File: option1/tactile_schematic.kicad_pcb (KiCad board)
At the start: 2 copper layers, 89.3 x 58.4 mm, 37 parts, among them IC1 CY8C4145PVI-PS431, J1 Conn_01x02, J2 Conn_01x04, J3 Conn_01x04, J4 Conn_01x02

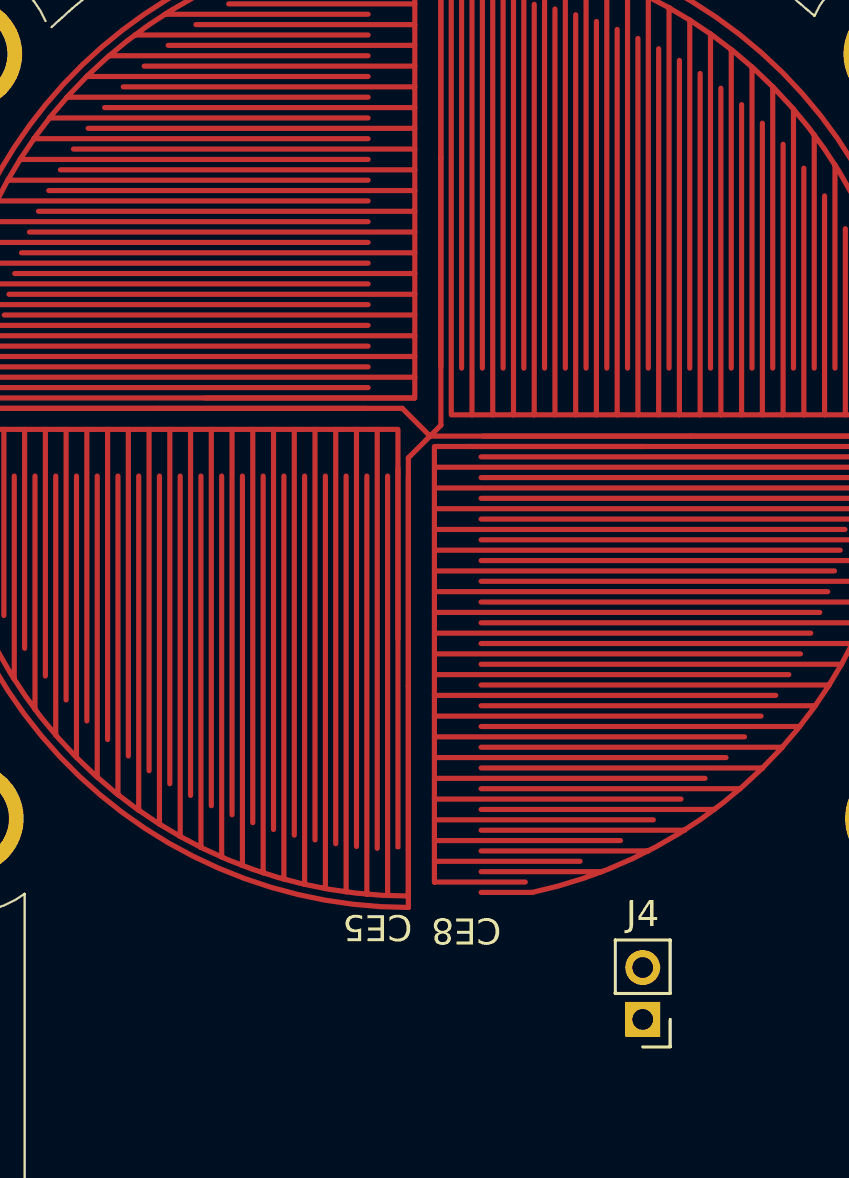
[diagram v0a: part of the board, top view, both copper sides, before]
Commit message: need to fix edge cuts not lining up
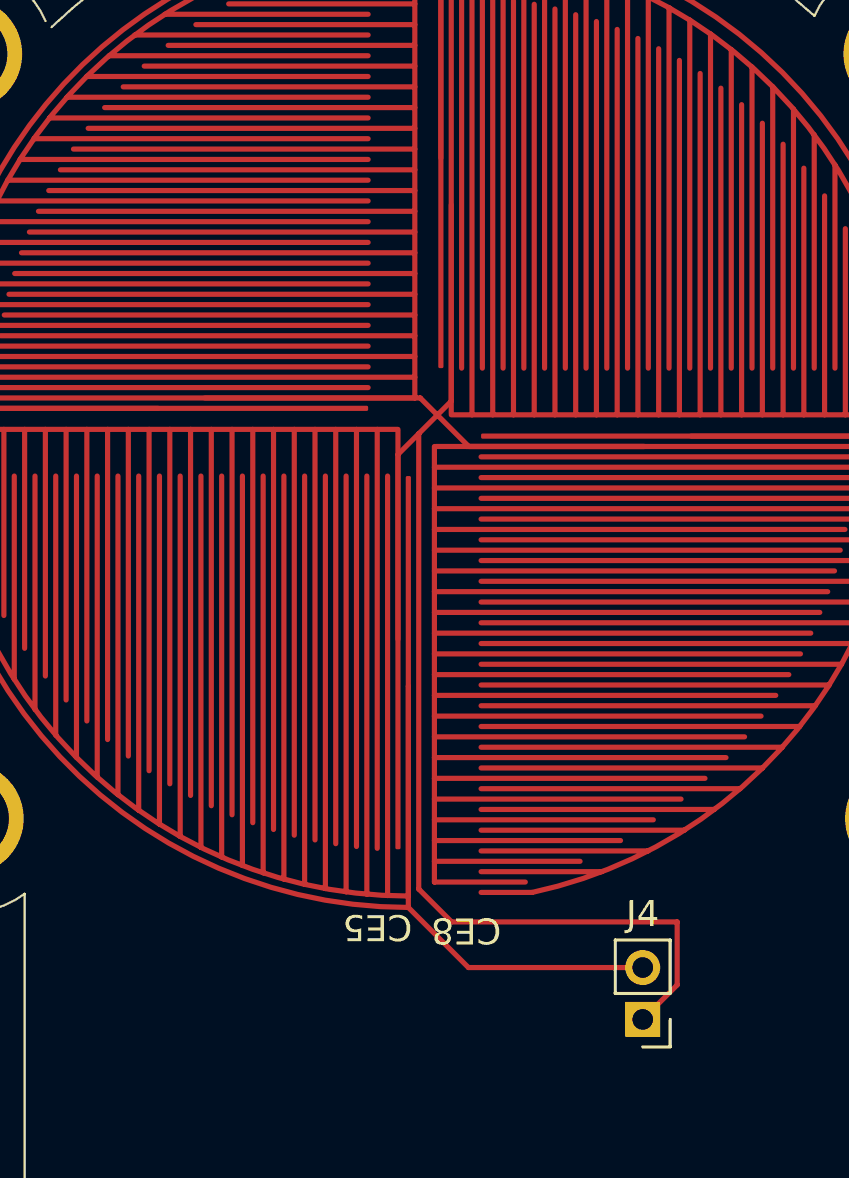
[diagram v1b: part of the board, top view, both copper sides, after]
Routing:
- net P5.2: track 30.3 -> 83.3 mm
- net P5.3: track 96.5 -> 64.7 mm
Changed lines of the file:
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@@
-	)
-	(segment
-		(start 242.08072 51.9999)
-		(end 242.91862 51.162)
-		(width 0.2)
-		(layer "F.Cu")
-		(net 5)
-	)
-	(segment
-		(start 243.33572 40.441)
-		(end 243.33572 50.7449)
-		(width 0.2)
-		(layer "F.Cu")
-		(net 5)
 	)
 	(segment
@@
 	)
 	(segment
-		(start 242.91862 51.162)
-		(end 252.98572 51.162)
-		(width 0.2)
-		(layer "F.Cu")
-		(net 5)
-	)
-	(segment
 		(start 223.908189 49.797789)
 		(end 223.8944 49.784)
@@
 	)
 	(segment
-		(start 243.33572 50.7449)
-		(end 242.91862 51.162)
-		(width 0.2)
-		(layer "F.Cu")
-		(net 5)
-	)
-	(segment
 		(start 243.33572 32.0548)
 		(end 238.5248 32.0548)
@@
 	(segment
 		(start 242.08072 60.802)
-		(end 242.08072 51.9999)
-		(width 0.2)
-		(layer "F.Cu")
-		(net 5)
-	)
-	(segment
-		(start 242.08072 60.802)
 		(end 242.0808 60.80208)
+		(width 0.2)
+		(layer "F.Cu")
+		(net 5)
+	)
+	(segment
+		(start 244.39872 71.66)
+		(end 242.08072 69.342)
 		(width 0.2)
 		(layer "F.Cu")
@@
 	)
 	(segment
+		(start 251.121 71.66)
+		(end 244.39872 71.66)
+		(width 0.2)
+		(layer "F.Cu")
+		(net 5)
+	)
+	(segment
 		(start 204.231 73.55)
 		(end 206.121 71.66)
@@
 	)
 	(segment
-		(start 241.84762 50.091)
-		(end 242.91862 51.162)
-		(width 0.2)
-		(layer "F.Cu")
-		(net 5)
-	)
-	(segment
-		(start 232.43072 50.091)
-		(end 241.84762 50.091)
-		(width 0.2)
-		(layer "F.Cu")
-		(net 5)
+		(start 243.73572 42.243)
+		(end 243.73572 49.81428)
+		(width 0.2)
+		(layer "F.Cu")
+		(net 6)
 	)
 	(segment
@@
 	)
 	(segment
-		(start 242.318 49.691)
-		(end 234.23272 49.691)
-		(width 0.2)
-		(layer "F.Cu")
-		(net 6)
-	)
-	(segment
-		(start 241.68072 52.3999)
-		(end 241.68072 59)
+		(start 243.2 50.35)
+		(end 244.412 51.562)
+		(width 0.2)
+		(layer "F.Cu")
+		(net 6)
+	)
+	(segment
+		(start 244.412 51.562)
+		(end 251.18372 51.562)
+		(width 0.2)
+		(layer "F.Cu")
+		(net 6)
+	)
+	(segment
+		(start 241.68072 59)
+		(end 241.68072 51.86928)
+		(width 0.2)
+		(layer "F.Cu")
+		(net 6)
+	)
+	(segment
+		(start 242.48172 51.08172)
+		(end 242.48172 68.63172)
+		(width 0.2)
+		(layer "F.Cu")
+		(net 6)
+	)
+	(segment
+		(start 234.23272 49.691)
+		(end 242.541 49.691)
+		(width 0.2)
+		(layer "F.Cu")
+		(net 6)
+	)
+	(segment
+		(start 243.73572 49.81428)
+		(end 243.2 50.35)
+		(width 0.2)
+		(layer "F.Cu")
+		(net 6)
+	)
+	(segment
+		(start 242.541 49.691)
+		(end 243.2 50.35)
 		(width 0.2)
 		(layer "F.Cu")
@@
 	)
 	(segment
+		(start 252.45 69.9)
+		(end 252.45 72.331)
+		(width 0.2)
+		(layer "F.Cu")
+		(net 6)
+	)
+	(segment
+		(start 242.475 51.075)
+		(end 242.48172 51.08172)
+		(width 0.2)
+		(layer "F.Cu")
+		(net 6)
+	)
+	(segment
+		(start 242.475 51.075)
+		(end 243.2 50.35)
+		(width 0.2)
+		(layer "F.Cu")
+		(net 6)
+	)
+	(segment
+		(start 252.45 72.331)
+		(end 251.121 73.66)
+		(width 0.2)
+		(layer "F.Cu")
+		(net 6)
+	)
+	(segment
 		(start 244.316 51.562)
 		(end 251.18372 51.562)
@@
 	)
 	(segment
+		(start 242.48172 68.63172)
+		(end 243.75 69.9)
+		(width 0.2)
+		(layer "F.Cu")
+		(net 6)
+	)
+	(segment
 		(start 206.121 73.66)
 		(end 205.581 74.2)
 		(width 0.2)
 		(layer "F.Cu")
+		(net 6)
+	)
+	(segment
+		(start 241.68072 51.86928)
+		(end 242.475 51.075)
+		(width 0.2)
+		(layer "F.Cu")
+		(net 6)
+	)
+	(segment
+		(start 243.75 69.9)
+		(end 252.45 69.9)
+		(width 0.2)
+		(layer "F.Cu")
